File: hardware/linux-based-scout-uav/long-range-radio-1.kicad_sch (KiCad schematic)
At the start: 1 part, among them U2 RN2903A-I_RM098

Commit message: Schematic update
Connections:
- net GND: now reaches U2.1 (GND), U2.11 (GND), U2.20 (GND), U2.21 (GND), U2.22 (GND), U2.24 (GND), U2.26 (GND), U2.27 (GND), U2.28 (GND), U2.33 (GND), U2.41 (GND), U2.47 (GND), U2.8 (GND)
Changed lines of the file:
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@@
 	(generator_version "8.0")
 	(paper "A3")
+	(wire
+		(pts
+			(xy 231.14 162.56) (xy 231.14 149.86)
+		)
+		(stroke
+			(width 0)
+			(type default)
+		)
+	)
+	(wire
+		(pts
+			(xy 231.14 149.86) (xy 223.52 149.86)
+		)
+		(stroke
+			(width 0)
+			(type default)
+		)
+	)
+	(symbol
+		(lib_id "power:GND")
+		(at 231.14 162.56 0)
+		(unit 1)
+		(exclude_from_sim no)
+		(in_bom yes)
+		(on_board yes)
+		(dnp no)
+		(fields_autoplaced yes)
+		(property "Reference" "#PWR014"
+			(at 231.14 168.91 0)
+			(effects
+				(font
+					(size 1.27 1.27)
+				)
+				(hide yes)
+			)
+		)
+		(property "Value" "GND"
+			(at 231.14 167.64 0)
+			(effects
+				(font
+					(size 1.27 1.27)
+				)
+			)
+		)
+		(property "Footprint" ""
+			(at 231.14 162.56 0)
+			(effects
+				(font
+					(size 1.27 1.27)
+				)
+				(hide yes)
+			)
+		)
+		(property "Datasheet" ""
+			(at 231.14 162.56 0)
+			(effects
+				(font
+					(size 1.27 1.27)
+				)
+				(hide yes)
+			)
+		)
+		(property "Description" "Power symbol creates a global label with name \"GND\" , ground"
+			(at 231.14 162.56 0)
+			(effects
+				(font
+					(size 1.27 1.27)
+				)
+				(hide yes)
+			)
+		)
+		(pin "1"
+		)
+		(instances
+			(project ""
+				(path "/e9b29a7c-bbe5-4ab4-acee-985586e1266a/ecf4917e-c539-4d94-9930-0d98be4d8645"
+					(reference "#PWR014")
+					(unit 1)
+				)
+			)
+		)
+	)
 	(symbol
 		(lib_id "RN2903A-I_RM098:RN2903A-I_RM098")

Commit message: Schematic update
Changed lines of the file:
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@@
+	(wire
+		(pts
+			(xy 223.52 111.76) (xy 250.19 111.76)
+		)
+		(stroke
+			(width 0)
+			(type default)
+		)
+	)
+	(wire
+		(pts
+			(xy 154.94 111.76) (xy 182.88 111.76)
+		)
+		(stroke
+			(width 0)
+			(type default)
+		)
+	)
 	(wire
 		(pts

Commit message: Schematic update
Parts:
- added L1: L, Inductor_SMD:L_0402_1005Metric, symbol Device:L
- added U7: SX1272, Package_DFN_QFN:QFN-28-1EP_6x6mm_P0.65mm_EP4.8x4.8mm_ThermalVias, symbol RF:SX1272
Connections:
- net GND: now also U7.16 (GND), U7.22 (GND), U7.26 (GND), U7.29 (GND)
- new net: L1.1, U7.27 (PA_BOOST)
- new net ~{SX1272_RESET}: U7.6 (~{RESET})
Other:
- note added: "Connect to OSD32MP1 GPIO"
- note added: "Long range radio"
- note added: "RN2903 LoRa module option"
- note added: "SX1272 LoRaWAN IC option"
- moved on the sheet: U2

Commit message: Schematic and Board update
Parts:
- added TP20, TP21, TP22, TP23, TP24: TestPoint, TestPoint:TestPoint_Pad_D1.0mm, symbol Connector:TestPoint
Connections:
- net at U2.35 (GPIO0): now also TP20.1
- net at U2.36 (GPIO1): now also TP21.1
- net at U2.37 (GPIO2): now also TP22.1
- net at U2.38 (GPIO3): now also TP23.1
- net at U2.39 (GPIO4): now also TP24.1
- net UART_TX: now reaches U2.6 (UART_TX)
- net UART_RX: now reaches U2.7 (UART_RX)
- no-connect marks 0 -> 2

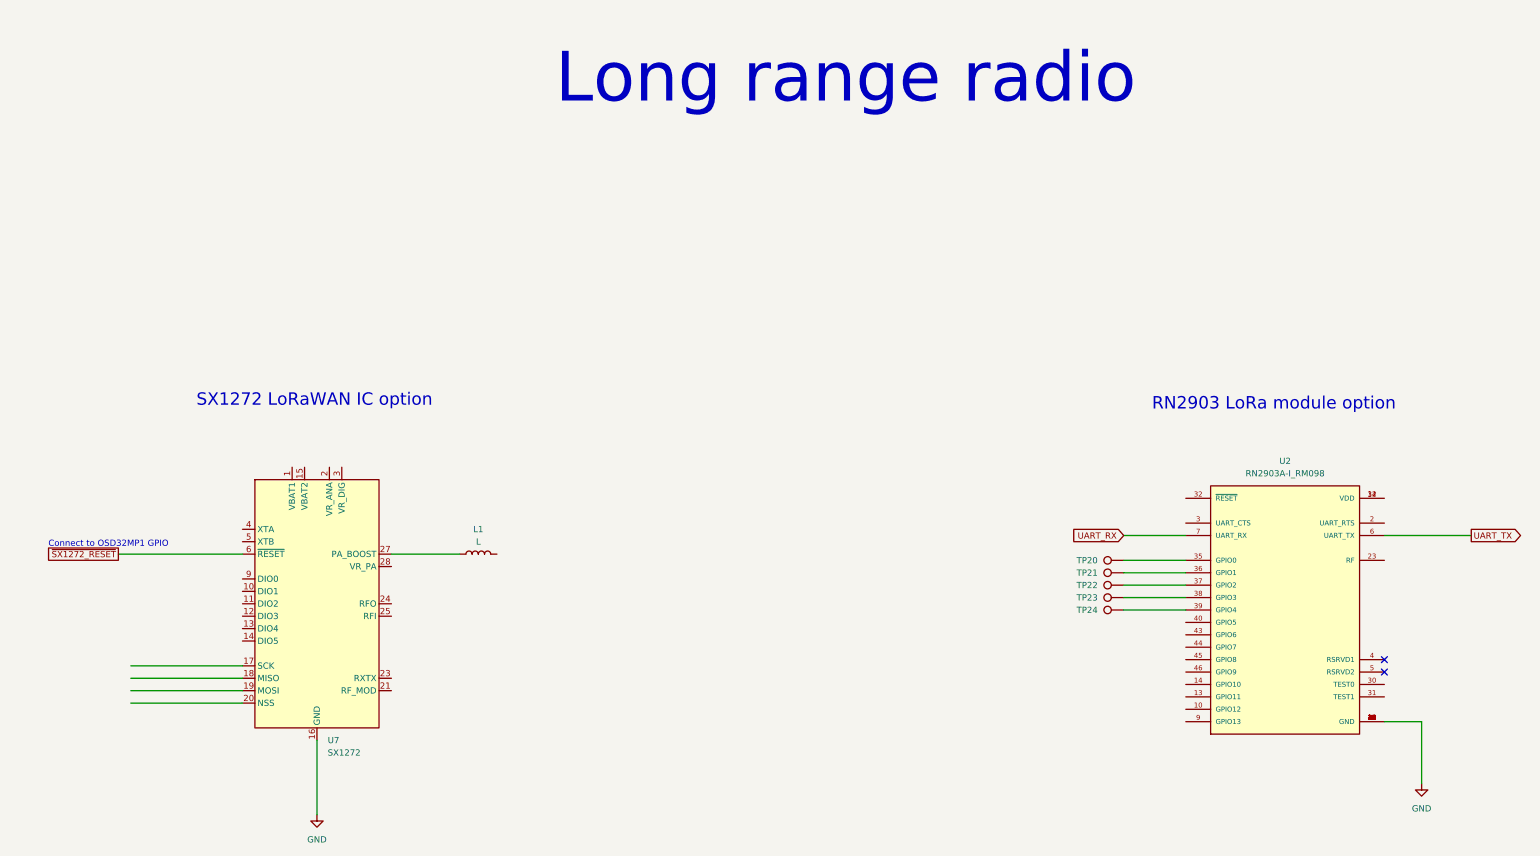
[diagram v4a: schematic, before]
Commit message: Updated project to KiCad 9.0
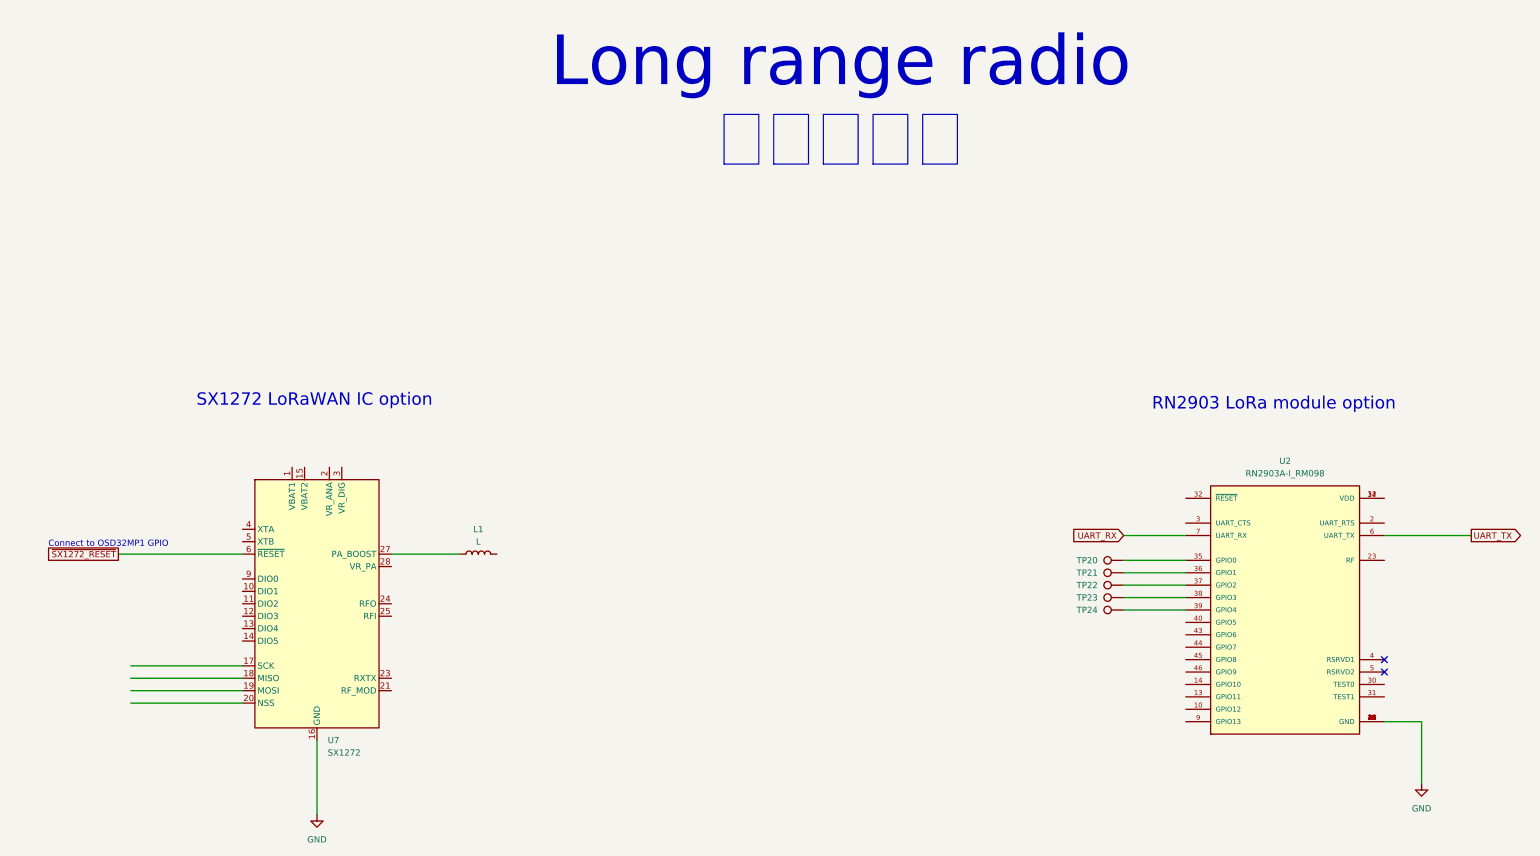
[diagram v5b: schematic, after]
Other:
- note added: "Long range radio 長距離無線"
- note removed: "Long range radio"
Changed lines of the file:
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@@
 (kicad_sch
-	(version 20231120)
+	(version 20250114)
 	(generator "eeschema")
-	(generator_version "8.0")
+	(generator_version "9.0")
 	(paper "A3")
+	(text "Connect to OSD32MP1 GPIO"
+		(exclude_from_sim no)
+		(at 64.008 118.618 0)
+		(effects
+			(font
+				(size 1.27 1.27)
+			)
+		)
+	)
+	(text "RN2903 LoRa module option"
+		(exclude_from_sim no)
+		(at 302.514 89.916 0)
+		(effects
+			(font
+				(size 2.54 2.54)
+			)
+		)
+	)
+	(text "Long range radio \n長距離無線"
+		(exclude_from_sim no)
+		(at 213.868 28.194 0)
+		(effects
+			(font
+				(size 10.16 10.16)
+			)
+		)
+	)
+	(text "SX1272 LoRaWAN IC option"
+		(exclude_from_sim no)
+		(at 106.172 89.154 0)
+		(effects
+			(font
+				(size 2.54 2.54)
+			)
+		)
+	)
 	(no_connect
 		(at 325.12 142.24)
@@
 		)
 	)
-	(text "Connect to OSD32MP1 GPIO"
-		(exclude_from_sim no)
-		(at 64.008 118.618 0)
-		(effects
-			(font
-				(size 1.27 1.27)
-			)
-		)
-	)
-	(text "RN2903 LoRa module option"
-		(exclude_from_sim no)
-		(at 302.514 89.916 0)
-		(effects
-			(font
-				(size 2.54 2.54)
-			)
-		)
-	)
-	(text "Long range radio "
-		(exclude_from_sim no)
-		(at 214.884 23.368 0)
-		(effects
-			(font
-				(size 10.16 10.16)
-			)
-		)
-	)
-	(text "SX1272 LoRaWAN IC option"
-		(exclude_from_sim no)
-		(at 106.172 89.154 0)
-		(effects
-			(font
-				(size 2.54 2.54)
-			)
-		)
-	)
